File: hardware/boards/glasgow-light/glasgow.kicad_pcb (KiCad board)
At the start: 2 copper layers, 64 x 20 mm, 172 parts, among them J1 USB_C_USB2.0, J2 IDC-Header_2x5_P2.54mm, J3 IDC-Header_2x5_P2.54mm, U1 LM358_DFN, U10 SN74LVC1T45DCKR, U11 SN74LVC1T45DCKR, U12 INA180A2, U15 TPD3S014, U16 SN74LVC1T45DCKR, U17 SN74LVC1T45DCKR, U18 SN74LVC1T45DCKR, U19 PCA6408APW, U2 GD32VF103T, U31 TPS73101DBV, U36 TLV73312PQDRVR, U4 SN74LVC1T45DCKR, U5 ICE40UP5K-SG48ITR, U6 SN74LVC1T45DCKR, U8 TLV75533PDRVR, U9 SN74LVC1T45DCKR, Y1 8M

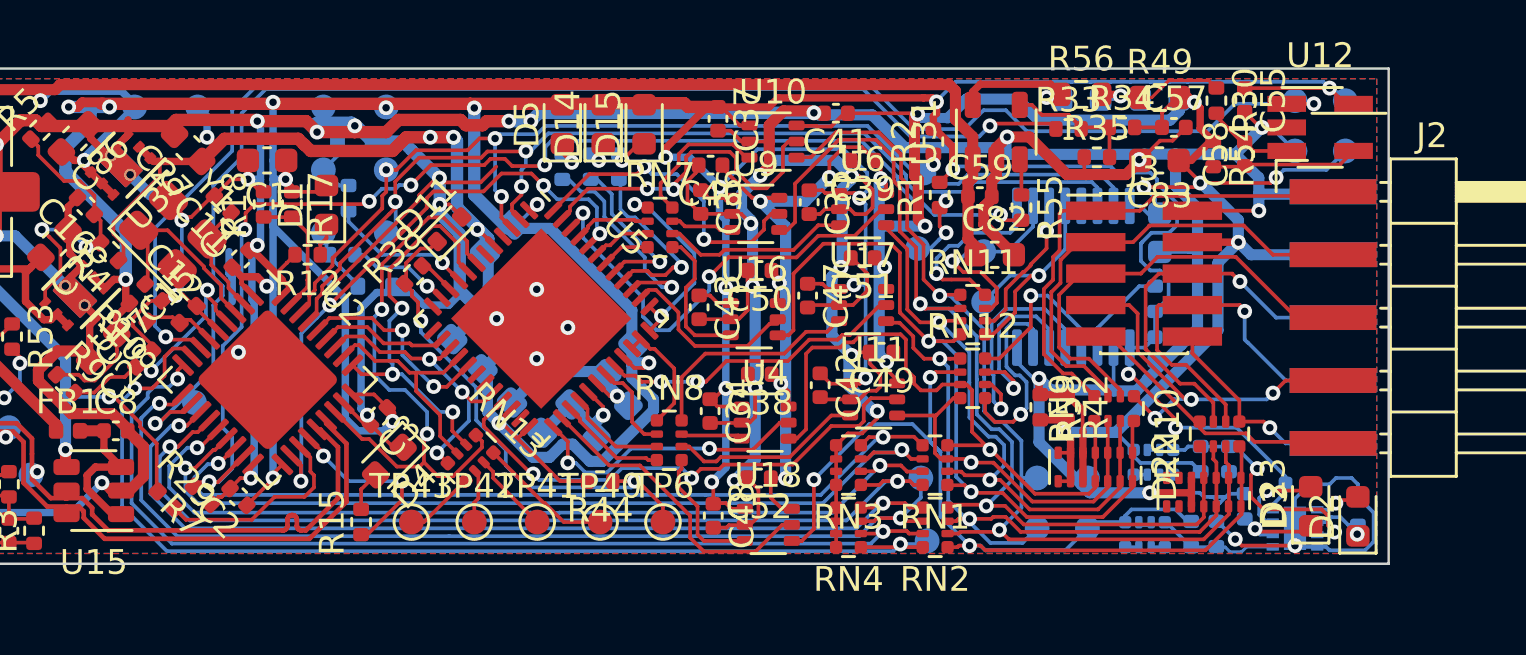
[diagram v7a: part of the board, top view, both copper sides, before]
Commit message: optimize location of test points
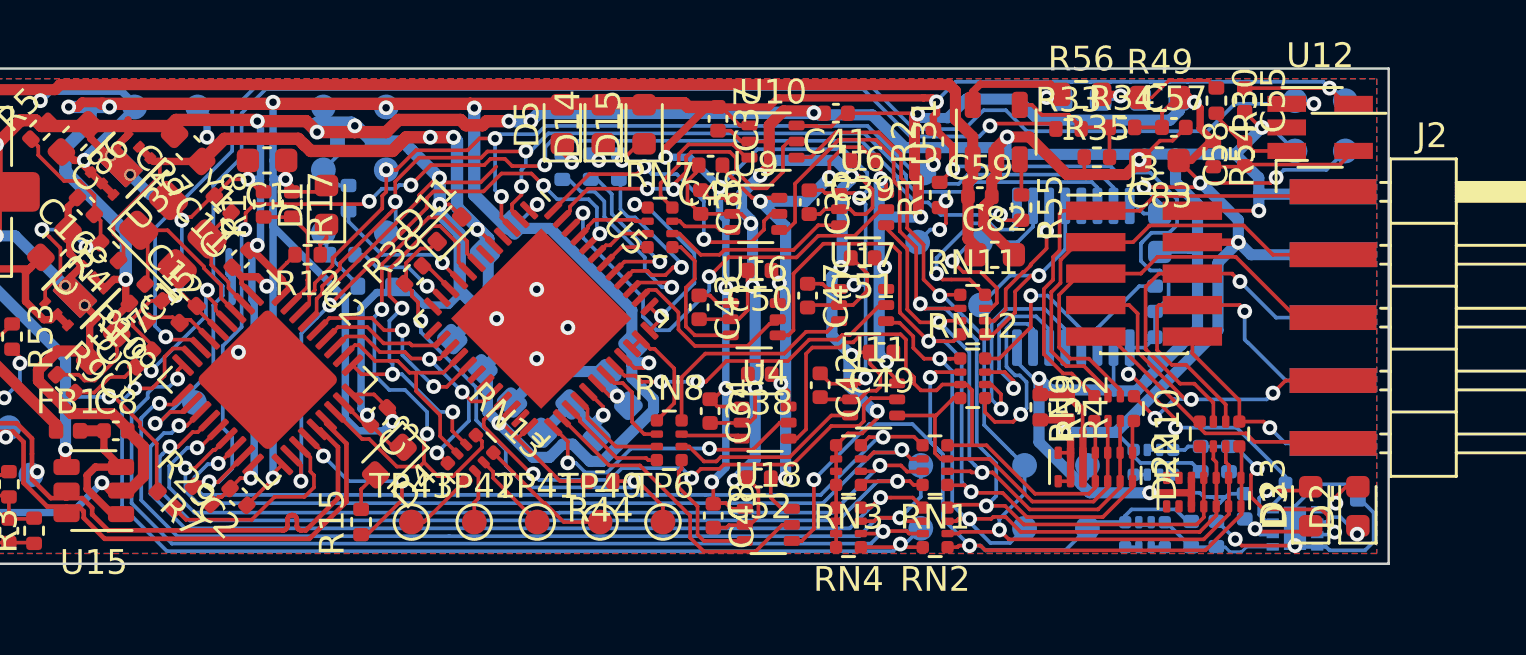
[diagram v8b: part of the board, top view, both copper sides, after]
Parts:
- moved TP27 0.72 mm to (159.5, 50.0)
- moved TP29 0.57 mm to (155.3, 52.6)
- moved TP26 0.51 mm to (159.5, 52.6)
- moved TP30 0.51 mm to (155.3, 50.0)
- moved TP31 0.51 mm to (162.1, 50.0)
- moved D2 0.41 mm to (173.0, 51.7)
- moved TP32 0.40 mm to (157.7, 41.0)
- moved TP4 0.25 mm to (155.2, 41.0)
- moved TP33 0.18 mm to (157.7, 43.6)
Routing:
- net /IO_Banks/IO_Buffer_A/Y2: track 24.6 -> 23.5 mm
- net /IO_Banks/IO_Buffer_A/Y6: track 39.3 -> 38.4 mm
- net /IO_Banks/IO_Buffer_A/Y4: track 40.1 -> 39.3 mm
- net /IO_Banks/IO_Buffer_A/P5: track 8.63 -> 8.09 mm
- net /IO_Banks/IO_Buffer_A/Y0: track 25.7 -> 25.2 mm, vias 1 -> 0
- net /IO_Banks/IO_Buffer_A/Y5: track 29.0 -> 28.5 mm
- net /IO_Banks/IO_Buffer_A/Y1: vias 1 -> 0
